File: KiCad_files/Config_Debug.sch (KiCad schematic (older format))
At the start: 73 parts, among them J12 Conn_01x03, J3 Conn_01x06, J4 USB_C_Receptacle, J8 Conn_01x02, J9 Conn_01x02, SW1 SW_Push, U1 XC7A35T_CSG325, U10 W25Q128JV, U6 FT2232HL, U7 93LCxxC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

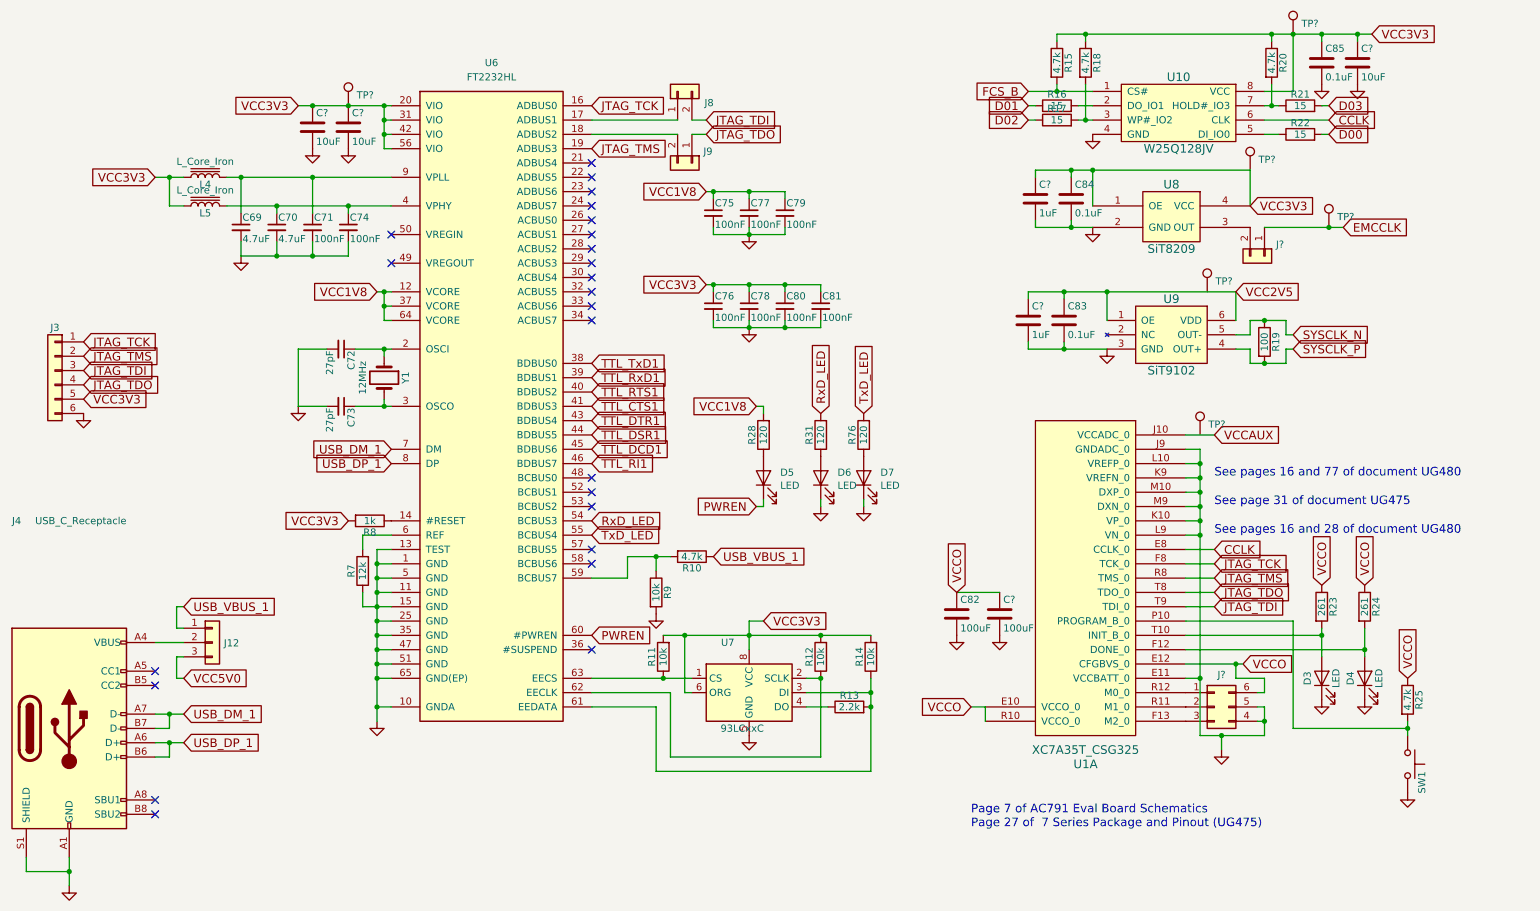
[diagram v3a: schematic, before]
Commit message: Annotations and proper connections
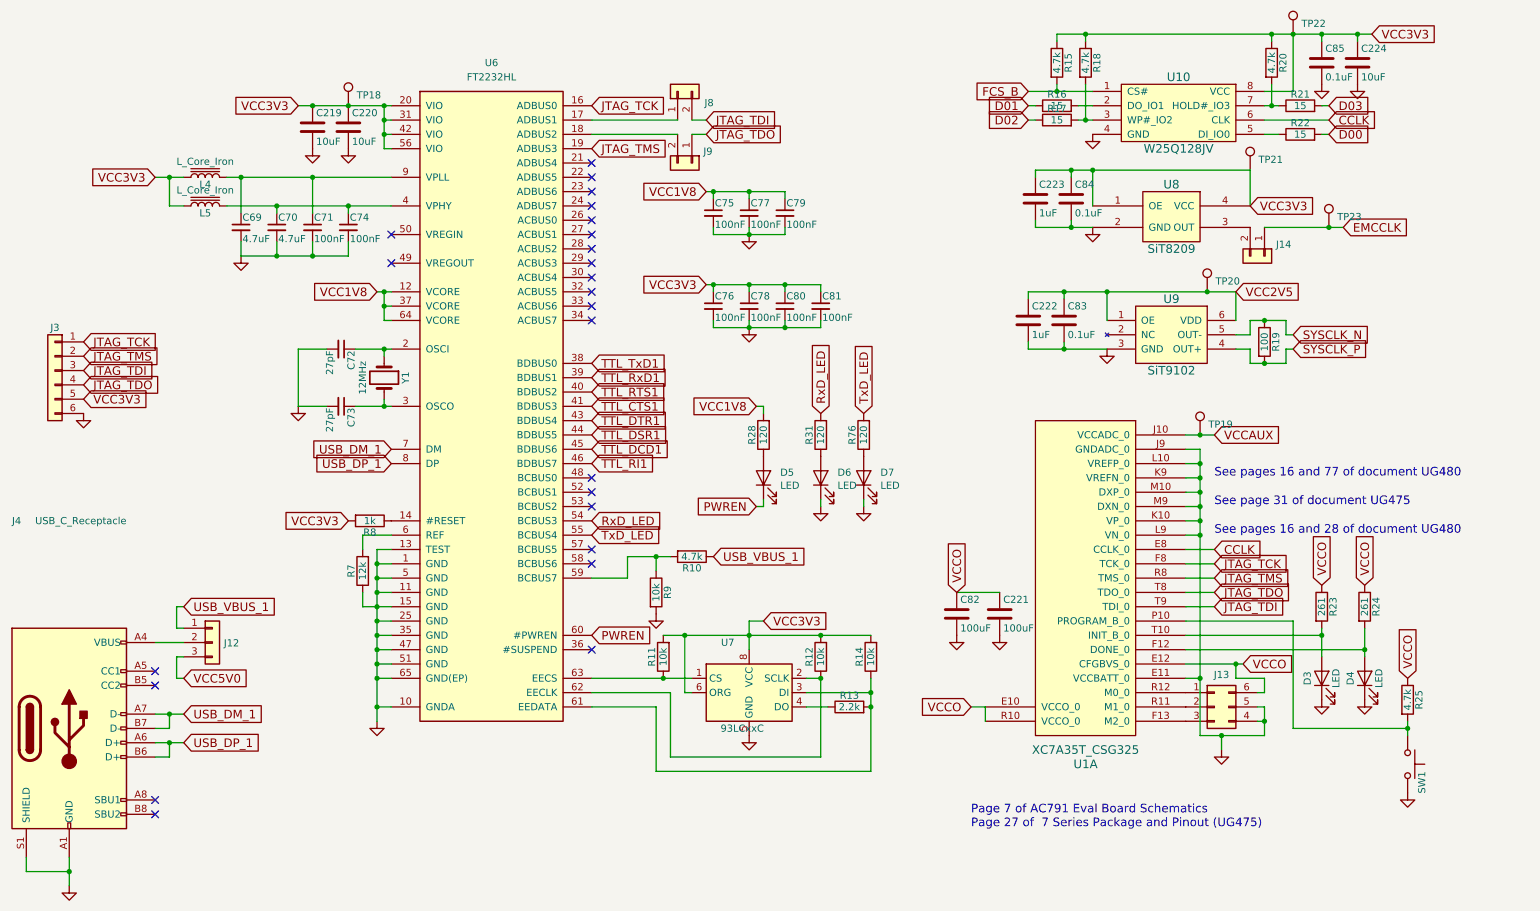
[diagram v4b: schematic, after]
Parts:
- gave numbers to parts that had none: 14
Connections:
- net VCC2V5: now also TP20.1
- net VCCAUX: now also TP19.1
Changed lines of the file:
@@
 	9200 4800 9000 4800
 Wire Wire Line
-	9000 3600 9200 3600
+	9000 3600 9100 3600
 Wire Wire Line
 	9000 3800 9100 3800
@@
 	8350 1750 9450 1750
 Wire Wire Line
-	8450 2600 9350 2600
+	8450 2600 9150 2600
 Wire Wire Line
 	9550 2800 9700 2800
@@
 P 7700 4850
 AR Path="/5C064F83/5C7A8FC9" Ref="C?"  Part="1"
-AR Path="/5C0630AC/5C7A8FC9" Ref="C?"  Part="1"
-F 0 "C?" H 7725 4950 50  0000 L CNN
+AR Path="/5C0630AC/5C7A8FC9" Ref="C221"  Part="1"
+F 0 "C221" H 7725 4950 50  0000 L CNN
 F 1 "100uF" H 7725 4750 50  0000 L CNN
 F 2 "" H 7738 4700 50  0001 C CNN
@@
 P 7700 5000
 AR Path="/5C064F83/5C7A8FD0" Ref="#PWR?"  Part="1"
-AR Path="/5C0630AC/5C7A8FD0" Ref="#PWR?"  Part="1"
-F 0 "#PWR?" H 7700 4750 50  0001 C CNN
+AR Path="/5C0630AC/5C7A8FD0" Ref="#PWR0137"  Part="1"
+F 0 "#PWR0137" H 7700 4750 50  0001 C CNN
 F 1 "GND" H 7700 4850 50  0001 C CNN
 F 2 "" H 7700 5000 50  0001 C CNN
@@
 	7400 4700 7700 4700
 $Comp
-L Device:C C?
+L Device:C C224
 U 1 1 5C7BFE87
 P 10200 1000
-F 0 "C?" H 10225 1100 50  0000 L CNN
+F 0 "C224" H 10225 1100 50  0000 L CNN
 F 1 "10uF" H 10225 900 50  0000 L CNN
 F 2 "" H 10238 850 50  0001 C CNN
@@
 $EndComp
 $Comp
-L power:GND #PWR?
+L power:GND #PWR0138
 U 1 1 5C7BFE8E
 P 10200 1150
-F 0 "#PWR?" H 10200 900 50  0001 C CNN
+F 0 "#PWR0138" H 10200 900 50  0001 C CNN
 F 1 "GND" H 10200 1000 50  0001 C CNN
 F 2 "" H 10200 1150 50  0001 C CNN
@@
 	10200 800  10300 800
 $Comp
-L Device:C C?
+L Device:C C222
 U 1 1 5C7EA238
 P 7900 2800
-F 0 "C?" H 7925 2900 50  0000 L CNN
+F 0 "C222" H 7925 2900 50  0000 L CNN
 F 1 "1uF" H 7925 2700 50  0000 L CNN
 F 2 "" H 7938 2650 50  0001 C CNN
@@
 Connection ~ 8150 2600
 $Comp
-L Device:C C?
+L Device:C C223
 U 1 1 5C81375F
 P 7950 1950
-F 0 "C?" H 7975 2050 50  0000 L CNN
+F 0 "C223" H 7975 2050 50  0000 L CNN
 F 1 "1uF" H 7975 1850 50  0000 L CNN
 F 2 "" H 7988 1800 50  0001 C CNN
@@
 Connection ~ 8200 2150
 $Comp
-L Device:C C?
+L Device:C C220
 U 1 1 5C83BC44
 P 3150 1450
-F 0 "C?" H 3175 1550 50  0000 L CNN
+F 0 "C220" H 3175 1550 50  0000 L CNN
 F 1 "10uF" H 3175 1350 50  0000 L CNN
 F 2 "" H 3188 1300 50  0001 C CNN
@@
 $EndComp
 $Comp
-L power:GND #PWR?
+L power:GND #PWR0136
 U 1 1 5C83BC4B
 P 3150 1600
-F 0 "#PWR?" H 3150 1350 50  0001 C CNN
+F 0 "#PWR0136" H 3150 1350 50  0001 C CNN
 F 1 "GND" H 3150 1450 50  0001 C CNN
 F 2 "" H 3150 1600 50  0001 C CNN
@@
 $EndComp
 $Comp
-L Device:C C?
+L Device:C C219
 U 1 1 5C84FF3B
 P 2900 1450
-F 0 "C?" H 2925 1550 50  0000 L CNN
+F 0 "C219" H 2925 1550 50  0000 L CNN
 F 1 "10uF" H 2925 1350 50  0000 L CNN
 F 2 "" H 2938 1300 50  0001 C CNN
@@
 $EndComp
 $Comp
-L power:GND #PWR?
+L power:GND #PWR0135
 U 1 1 5C84FF42
 P 2900 1600
-F 0 "#PWR?" H 2900 1350 50  0001 C CNN
+F 0 "#PWR0135" H 2900 1350 50  0001 C CNN
 F 1 "GND" H 2900 1450 50  0001 C CNN
 F 2 "" H 2900 1600 50  0001 C CNN
@@
 	3150 1300 3400 1300
 $Comp
-L Connector_Generic:Conn_01x02 J?
+L Connector_Generic:Conn_01x02 J14
 U 1 1 5C87AC76
 P 9550 2350
-F 0 "J?" V 9469 2430 50  0000 L CNN
+F 0 "J14" V 9469 2430 50  0000 L CNN
 F 1 "Conn_01x02" V 9514 2430 50  0001 L CNN
 F 2 "" H 9550 2350 50  0001 C CNN
@@
 $EndComp
 $Comp
-L Connector_Generic:Conn_02x03_Counter_Clockwise J?
+L Connector_Generic:Conn_02x03_Counter_Clockwise J13
 U 1 1 5C8D400A
 P 9200 5500
-F 0 "J?" H 9250 5725 50  0000 C CNN
+F 0 "J13" H 9250 5725 50  0000 C CNN
 F 1 "Conn_02x03_Counter_Clockwise" H 9250 5726 50  0001 C CNN
 F 2 "" H 9200 5500 50  0001 C CNN
@@
 P 3150 1300
 AR Path="/5BFDDAF0/5CDCFA60" Ref="TP?"  Part="1"
-AR Path="/5C0630AC/5CDCFA60" Ref="TP?"  Part="1"
-F 0 "TP?" H 3208 1374 50  0000 L CNN
+AR Path="/5C0630AC/5CDCFA60" Ref="TP18"  Part="1"
+F 0 "TP18" H 3208 1374 50  0000 L CNN
 F 1 "TestPoint" H 3208 1329 50  0001 L CNN
 F 2 "" H 3350 1300 50  0001 C CNN
@@
 P 9100 3600
 AR Path="/5BFDDAF0/5CDE48B6" Ref="TP?"  Part="1"
-AR Path="/5C0630AC/5CDE48B6" Ref="TP?"  Part="1"
-F 0 "TP?" H 9158 3674 50  0000 L CNN
+AR Path="/5C0630AC/5CDE48B6" Ref="TP19"  Part="1"
+F 0 "TP19" H 9158 3674 50  0000 L CNN
 F 1 "TestPoint" H 9158 3629 50  0001 L CNN
 F 2 "" H 9300 3600 50  0001 C CNN
@@
 P 9750 800
 AR Path="/5BFDDAF0/5CDF99BD" Ref="TP?"  Part="1"
-AR Path="/5C0630AC/5CDF99BD" Ref="TP?"  Part="1"
-F 0 "TP?" H 9808 874 50  0000 L CNN
+AR Path="/5C0630AC/5CDF99BD" Ref="TP22"  Part="1"
+F 0 "TP22" H 9808 874 50  0000 L CNN
 F 1 "TestPoint" H 9808 829 50  0001 L CNN
 F 2 "" H 9950 800 50  0001 C CNN
@@
 P 9450 1750
 AR Path="/5BFDDAF0/5CE0E801" Ref="TP?"  Part="1"
-AR Path="/5C0630AC/5CE0E801" Ref="TP?"  Part="1"
-F 0 "TP?" H 9508 1824 50  0000 L CNN
+AR Path="/5C0630AC/5CE0E801" Ref="TP21"  Part="1"
+F 0 "TP21" H 9508 1824 50  0000 L CNN
 F 1 "TestPoint" H 9508 1779 50  0001 L CNN
 F 2 "" H 9650 1750 50  0001 C CNN
@@
 P 9150 2600
 AR Path="/5BFDDAF0/5CE384ED" Ref="TP?"  Part="1"
-AR Path="/5C0630AC/5CE384ED" Ref="TP?"  Part="1"
-F 0 "TP?" H 9208 2674 50  0000 L CNN
+AR Path="/5C0630AC/5CE384ED" Ref="TP20"  Part="1"
+F 0 "TP20" H 9208 2674 50  0000 L CNN
 F 1 "TestPoint" H 9208 2629 50  0001 L CNN
 F 2 "" H 9350 2600 50  0001 C CNN
@@
 U 1 1 5CE6965B
 P 10000 2150
-F 0 "TP?" H 10058 2224 50  0000 L CNN
+AR Path="/5BFDDAF0/5CE6965B" Ref="TP?"  Part="1"
+AR Path="/5C0630AC/5CE6965B" Ref="TP23"  Part="1"
+F 0 "TP23" H 10058 2224 50  0000 L CNN
 F 1 "TestPoint" H 10058 2179 50  0001 L CNN
 F 2 "" H 10200 2150 50  0001 C CNN
@@
 Wire Wire Line
 	10000 2150 10100 2150
+Connection ~ 9100 3600
+Wire Wire Line
+	9100 3600 9200 3600
+Connection ~ 9150 2600
+Wire Wire Line
+	9150 2600 9350 2600
 $EndSCHEMATC
